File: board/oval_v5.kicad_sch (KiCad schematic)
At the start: 122 parts, among them J1 HDR-5x1, J10 HDR-4x1, J11 HDR-4x1, J12 HDR-4x1, J13 HDR-4x1, J14 HDR-4x1, J15 HDR-4x1, J16 HDR-4x1, J17 HDR-4x1, J18 Conn_Coaxial, J19 Conn_01x02, J2 HDR-4x1, J20 Conn_01x02, J21 Conn_02x02_Counter_Clockwise, J22 HDR-2x1, J23 HDR-2x1, J25 Conn_01x06, J3 HDR-4x1, J4 Conn_01x06, J5 Micro_SD_Card, J6 Conn_01x02, J7 HDR-4x1, J8 Conn_01x08, J9 HDR-4x1, P1 USB_C_Plug_USB2.0, Q1 Q_PMOS_GSD, Q2 MMBT3904, Q3 MMBT3904, SW1 SW_DIP_x02, SW2 SW_DIP_x02, U1 RV-8803, U10 SiP32431DR3, U11 SiP32431DR3, U12 SiP32431DR3, U13 SiP32431DR3, U14 SiP32431DR3, U15 PCF8574TS, U16 PCA9548APW, U17 SiP32431DR3, U2 ESP32-S3-WROOM-1, U3 TMP117xxDRV, U4 RFM95W-915S2, U7 MAX3485, U8 AP7361C-33E, U9 AP7361C-33E

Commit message: minor changes
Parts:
- D5: footprint Diode_SMD:D_SOD-323 -> Diode_SMD:D_SOD-323_HandSoldering
- J20: footprint Connector_PinHeader_2.54mm:PinHeader_1x02_P2.54mm_Vertical -> Connector_JST:JST_XH_B2B-XH-A_1x02_P2.50mm_Vertical
- J25, J4: footprint Connector_PinHeader_2.54mm:PinHeader_1x06_P2.54mm_Vertical -> Connector_JST:JST_XH_B6B-XH-A_1x06_P2.50mm_Vertical
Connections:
- net CLK is gone; now on net SPI_SCLK: R4.1, U4.4 (SCK)
- net MISO is gone; now on net SPI_MISO: R5.1, U4.2 (MISO)
- net MOSI is gone; now on net SPI_MOSI: R3.1, U4.3 (MOSI)
- net SIM_PWRKEY is gone; now on net GSM_PWRKEY: J25.3 (Pin_3)
- net SIM_RST is gone; now on net GSM_RST: J25.4 (Pin_4)
- net SIM_RX is gone; now on net GSM_Rx: J25.2 (Pin_2)
- net SIM_TX is gone; now on net GSM_Tx: J25.1 (Pin_1)
- net GSM_Rx: now also U2.10 (GPIO17/U1TXD/ADC2_CH6)
- net GSM_Tx: now also U2.11 (GPIO18/U1RXD/ADC2_CH7/CLK_OUT3)
- net RS485_EN: now also U2.25 (GPIO48/SPICLK_N/SUBSPICLK_N_DIFF)
- net rfm_RST: now also U2.5 (GPIO5/TOUCH5/ADC1_CH4); no longer U2.10 (GPIO17/U1TXD/ADC2_CH6)
- net rfm_dio1: now also U2.24 (GPIO47/SPICLK_P/SUBSPICLK_P_DIFF); no longer U2.11 (GPIO18/U1RXD/ADC2_CH7/CLK_OUT3)
- net rfm_dio2: now also U2.6 (GPIO6/TOUCH6/ADC1_CH5), U4.16 (DIO2); no longer U2.31 (GPIO38/FSPIWP/SUBSPIWP)
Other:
- moved on the sheet: J18, U4

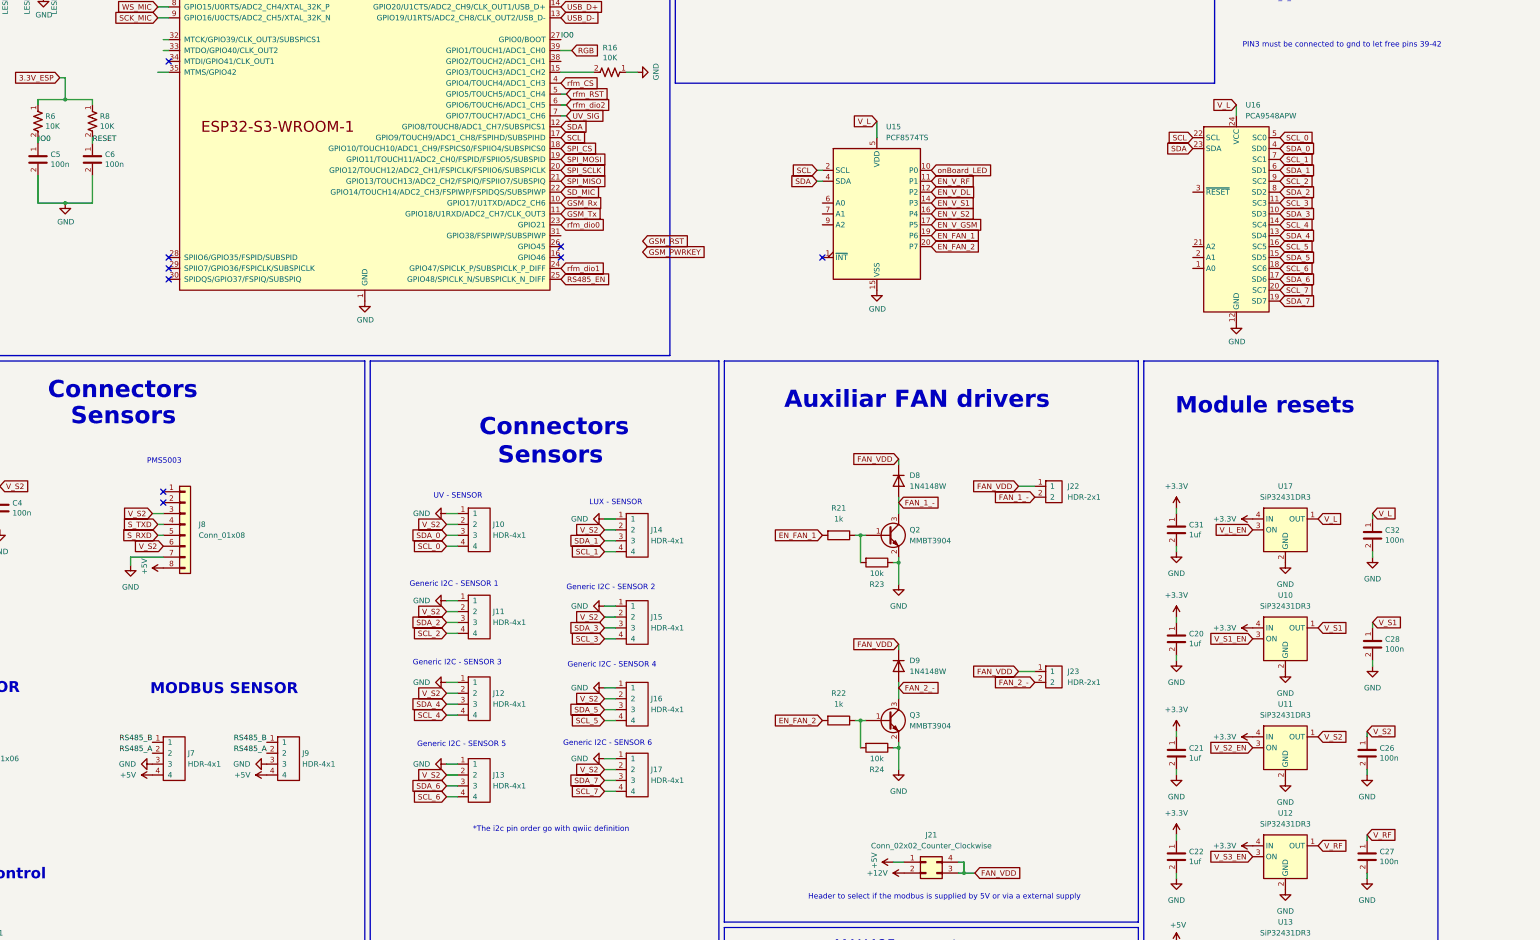
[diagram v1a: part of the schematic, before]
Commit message: working on layout -  defining connectors and cables
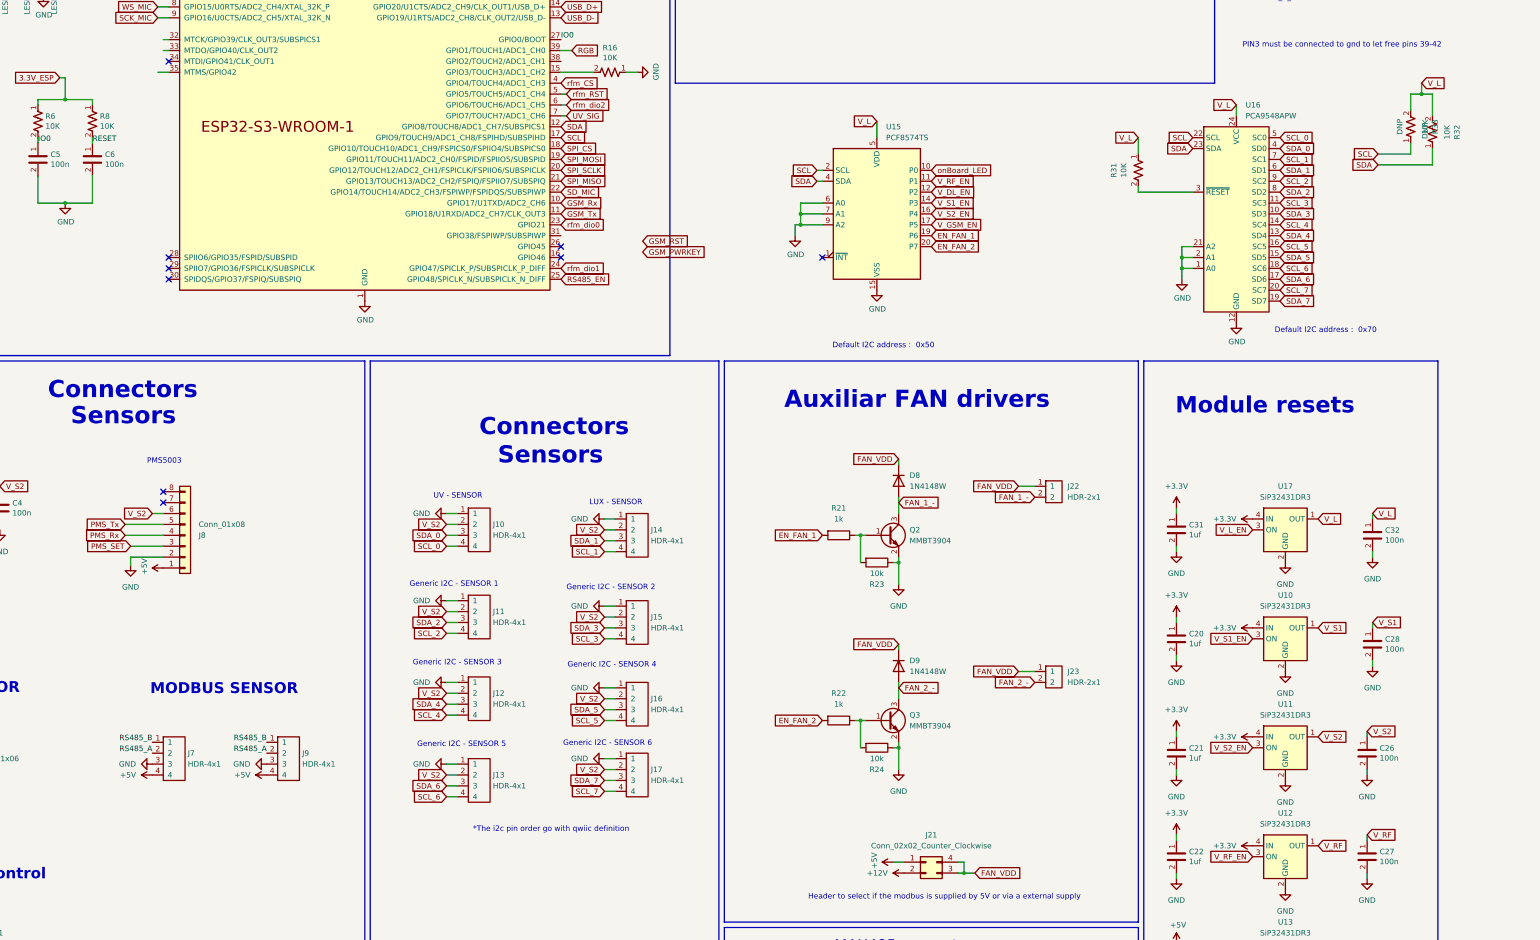
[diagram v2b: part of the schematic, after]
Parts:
- added R31, R32, R33: 10K, Resistor_SMD:R_0603_1608Metric, symbol IoWLabs:RES
- J4: footprint Connector_JST:JST_XH_B6B-XH-A_1x06_P2.50mm_Vertical -> Connector_JST:JST_GH_SM06B-GHS-TB_1x06-1MP_P1.25mm_Horizontal
- J8: footprint Connector_JST:JST_GH_SM08B-GHS-TB_1x08-1MP_P1.25mm_Horizontal -> Connector_Molex:Molex_PicoBlade_53261-0871_1x08-1MP_P1.25mm_Horizontal
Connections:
- net EN_V_DL is gone; now on net V_DL_EN: U15.12 (P2)
- net EN_V_GSM is gone; now on net V_GSM_EN: U15.17 (P5)
- net EN_V_S1 is gone; now on net V_S1_EN: U15.14 (P3)
- net EN_V_S2 is gone; now on net V_S2_EN: U15.16 (P4)
- net V_S3_EN is gone; now on net V_RF_EN: U12.3 (ON)
- net +5V: now also J8.1 (Pin_1); no longer J8.8 (Pin_8)
- net GND: now also J8.2 (Pin_2), U15.6 (A0), U15.7 (A1), U15.9 (A2), U16.1 (A0), U16.2 (A1), U16.21 (A2); no longer J8.7 (Pin_7)
- net SCL: now also R33.1
- net SDA: now also R32.1
- net V_L: now also R31.1, R32.2, R33.2
- net V_S2: no longer J8.3 (Pin_3)
- net at U16.3 (~{RESET}): now also R31.2
- net EN_V_RF renamed V_RF_EN
- net S_RXD renamed PMS_Tx
- net S_TXD renamed PMS_Rx
- new net PMS_SET: J8.3 (Pin_3)
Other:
- note added: "Default I2C address : 0x50"
- note added: "Default I2C address : 0x70"

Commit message: assignint pines
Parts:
- removed U15: PCF8574TS, Package_SO:SSOP-20_4.4x6.5mm_P0.65mm, symbol Interface_Expansion:PCF8574TS
- added C33: 100n, Capacitor_SMD:C_0603_1608Metric, symbol IoWLabs:C
- added C34: 10u, Capacitor_SMD:C_0805_2012Metric, symbol IoWLabs:C
- added R34, R35: 10k, Resistor_SMD:R_0603_1608Metric, symbol Device:R
- added R36, R37: 10K, Resistor_SMD:R_0603_1608Metric, symbol IoWLabs:RES
- added U18: PCA9555PW, Package_SO:TSSOP-24_4.4x7.8mm_P0.65mm, symbol Interface_Expansion:PCA9555PW
- R10, R11: value 2.2k -> 10k
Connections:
- net SPI_CS is gone; now on net SD_CS: U2.18 (GPIO10/TOUCH10/ADC1_CH9/FSPICS0/FSPIIO4/SUBSPICS0)
- net EN_FAN_1: now also U18.10 (IO0_6)
- net EN_FAN_2: now also U18.11 (IO0_7)
- net GND: now also C33.2, C34.2, U18.12 (VSS), U18.2 (A1), U18.21 (A0), U18.3 (A2)
- net GSM_PWRKEY: now also U2.6 (GPIO6/TOUCH6/ADC1_CH5)
- net GSM_RST: now also U2.5 (GPIO5/TOUCH5/ADC1_CH4)
- net PMS_Rx: now also U2.35 (MTMS/GPIO42)
- net PMS_SET: now also U18.13 (IO1_0)
- net PMS_Tx: now also U2.34 (MTDI/GPIO41/CLK_OUT1)
- net RS485_EN: now also U18.14 (IO1_1); no longer U2.25 (GPIO48/SPICLK_N/SUBSPICLK_N_DIFF)
- net SCL: now also R35.2, R36.1, U18.22 (SCL)
- net SDA: now also R34.2, R37.1, U18.23 (SDA)
- net V_DL_EN: now also U18.6 (IO0_2)
- net V_GSM_EN: now also U18.9 (IO0_5)
- net V_L: now also C33.1, C34.1, R36.2, R37.2, U18.24 (VDD)
- net V_RF_EN: now also U18.5 (IO0_1)
- net V_S1_EN: now also U18.7 (IO0_3)
- net V_S2: now also R34.1, R35.1
- net V_S2_EN: now also U18.8 (IO0_4)
- net onBoard_LED: now also U18.4 (IO0_0)
- net rfm_CS: now also U2.33 (MTDO/GPIO40/CLK_OUT2); no longer U2.4 (GPIO4/TOUCH4/ADC1_CH3)
- net rfm_RST: now also U2.32 (MTCK/GPIO39/CLK_OUT3/SUBSPICS1); no longer U2.5 (GPIO5/TOUCH5/ADC1_CH4)
- net rfm_dio0: now also U2.31 (GPIO38/FSPIWP/SUBSPIWP); no longer U2.23 (GPIO21)
- net rfm_dio2: now also U2.25 (GPIO48/SPICLK_N/SUBSPICLK_N_DIFF); no longer U2.6 (GPIO6/TOUCH6/ADC1_CH5)
- no-connect marks 23 -> 21
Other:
- note added: "Default I2C address : 0x20"
- note removed: "Default I2C address : 0x50"
- moved on the sheet: C5, C6, J4, J7, J9, R6, R8

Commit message: updateing 27/02
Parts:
- J1: footprint Connector_JST:JST_XH_B5B-XH-A_1x05_P2.50mm_Vertical -> Connector_JST:JST_PH_B5B-PH-K_1x05_P2.00mm_Vertical
- J10, J11, J12, J13, J14, J15, J16, J17: footprint Connector_JST:JST_SH_BM04B-SRSS-TB_1x04-1MP_P1.00mm_Vertical -> Connector_JST:JST_PH_B4B-PH-K_1x04_P2.00mm_Vertical
- J2, J3: footprint Connector_JST:JST_XH_B4B-XH-A_1x04_P2.50mm_Vertical -> Connector_JST:JST_SH_BM04B-SRSS-TB_1x04-1MP_P1.00mm_Vertical
- J20: footprint Connector_JST:JST_XH_B2B-XH-A_1x02_P2.50mm_Vertical -> Connector_JST:JST_PH_B2B-PH-K_1x02_P2.00mm_Vertical
- J22, J23: footprint Connector_JST:JST_XH_B2B-XH-A_1x02_P2.50mm_Vertical -> Connector_JST:JST_PH_S2B-PH-SM4-TB_1x02-1MP_P2.00mm_Horizontal
- J7, J9: footprint Connector_JST:JST_XH_B4B-XH-A_1x04_P2.50mm_Vertical -> Connector_JST:JST_PH_B4B-PH-K_1x04_P2.00mm_Vertical
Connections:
- net V_L_EN: now also U2.23 (GPIO21)
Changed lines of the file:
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@@
 		)
 	)
+	(global_label "V_L_EN"
+		(shape input)
+		(at 187.96 134.62 0)
+		(fields_autoplaced yes)
+		(effects
+			(font
+				(size 1.27 1.27)
+			)
+			(justify left)
+		)
+		(property "Intersheetrefs" "${INTERSHEET_REFS}"
+			(at 197.4766 134.62 0)
+			(effects
+				(font
+					(size 1.27 1.27)
+				)
+				(justify left)
+				(hide yes)
+			)
+		)
+	)
 	(global_label "V_RF"
 		(shape input)
@@
 			)
 		)
-		(property "Footprint" "Connector_JST:JST_SH_BM04B-SRSS-TB_1x04-1MP_P1.00mm_Vertical"
+		(property "Footprint" "Connector_JST:JST_PH_B4B-PH-K_1x04_P2.00mm_Vertical"
 			(at 207.01 200.66 0)
 			(effects
@@
 			)
 		)
-		(property "Footprint" "Connector_JST:JST_SH_BM04B-SRSS-TB_1x04-1MP_P1.00mm_Vertical"
+		(property "Footprint" "Connector_JST:JST_PH_B4B-PH-K_1x04_P2.00mm_Vertical"
 			(at 170.18 238.76 0)
 			(effects
@@
 			)
 		)
-		(property "Footprint" "Connector_JST:JST_SH_BM04B-SRSS-TB_1x04-1MP_P1.00mm_Vertical"
+		(property "Footprint" "Connector_JST:JST_PH_B4B-PH-K_1x04_P2.00mm_Vertical"
 			(at 207.01 256.54 0)
 			(effects
@@
 			)
 		)
-		(property "Footprint" "Connector_JST:JST_XH_B4B-XH-A_1x04_P2.50mm_Vertical"
+		(property "Footprint" "Connector_JST:JST_PH_B4B-PH-K_1x04_P2.00mm_Vertical"
 			(at 101.6 251.46 0)
 			(effects
@@
 			)
 		)
-		(property "Footprint" "Connector_JST:JST_XH_B4B-XH-A_1x04_P2.50mm_Vertical"
+		(property "Footprint" "Connector_JST:JST_PH_B4B-PH-K_1x04_P2.00mm_Vertical"
 			(at 128.27 251.46 0)
 			(effects
@@
 			)
 		)
-		(property "Footprint" "Connector_JST:JST_SH_BM04B-SRSS-TB_1x04-1MP_P1.00mm_Vertical"
+		(property "Footprint" "Connector_JST:JST_PH_B4B-PH-K_1x04_P2.00mm_Vertical"
 			(at 170.18 257.81 0)
 			(effects
@@
 			)
 		)
-		(property "Footprint" "Connector_JST:JST_SH_BM04B-SRSS-TB_1x04-1MP_P1.00mm_Vertical"
+		(property "Footprint" "Connector_JST:JST_PH_B4B-PH-K_1x04_P2.00mm_Vertical"
 			(at 170.18 199.39 0)
 			(effects
@@
 			)
 		)
-		(property "Footprint" "Connector_JST:JST_XH_B2B-XH-A_1x02_P2.50mm_Vertical"
+		(property "Footprint" "Connector_JST:JST_PH_S2B-PH-SM4-TB_1x02-1MP_P2.00mm_Horizontal"
 			(at 302.26 236.22 0)
 			(effects
@@
 			)
 		)
-		(property "Footprint" "Connector_JST:JST_SH_BM04B-SRSS-TB_1x04-1MP_P1.00mm_Vertical"
+		(property "Footprint" "Connector_JST:JST_PH_B4B-PH-K_1x04_P2.00mm_Vertical"
 			(at 207.01 220.98 0)
 			(effects
@@
 			)
 		)
-		(property "Footprint" "Connector_JST:JST_SH_BM04B-SRSS-TB_1x04-1MP_P1.00mm_Vertical"
+		(property "Footprint" "Connector_JST:JST_PH_B4B-PH-K_1x04_P2.00mm_Vertical"
 			(at 170.18 219.71 0)
 			(effects
@@
 			)
 		)
-		(property "Footprint" "Connector_JST:JST_XH_B4B-XH-A_1x04_P2.50mm_Vertical"
+		(property "Footprint" "Connector_JST:JST_SH_BM04B-SRSS-TB_1x04-1MP_P1.00mm_Vertical"
 			(at 46.99 219.71 0)
 			(effects
@@
 			)
 		)
-		(property "Footprint" "Connector_JST:JST_XH_B2B-XH-A_1x02_P2.50mm_Vertical"
+		(property "Footprint" "Connector_JST:JST_PH_S2B-PH-SM4-TB_1x02-1MP_P2.00mm_Horizontal"
 			(at 302.26 193.04 0)
 			(effects
@@
 			)
 		)
-		(property "Footprint" "Connector_JST:JST_SH_BM04B-SRSS-TB_1x04-1MP_P1.00mm_Vertical"
+		(property "Footprint" "Connector_JST:JST_PH_B4B-PH-K_1x04_P2.00mm_Vertical"
 			(at 207.01 240.03 0)
 			(effects
@@
 			)
 		)
-		(property "Footprint" "Connector_JST:JST_XH_B2B-XH-A_1x02_P2.50mm_Vertical"
+		(property "Footprint" "Connector_JST:JST_PH_B2B-PH-K_1x02_P2.00mm_Vertical"
 			(at 269.24 35.56 0)
 			(effects
@@
 			)
 		)
-		(property "Footprint" "Connector_JST:JST_XH_B5B-XH-A_1x05_P2.50mm_Vertical"
+		(property "Footprint" "Connector_JST:JST_PH_B5B-PH-K_1x05_P2.00mm_Vertical"
 			(at 44.45 209.55 0)
 			(effects
@@
 			)
 		)
-		(property "Footprint" "Connector_JST:JST_XH_B4B-XH-A_1x04_P2.50mm_Vertical"
+		(property "Footprint" "Connector_JST:JST_SH_BM04B-SRSS-TB_1x04-1MP_P1.00mm_Vertical"
 			(at 48.26 292.1 0)
 			(effects

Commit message: adding layout review
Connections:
- net GSM_PWRKEY: now also U2.35 (MTMS/GPIO42); no longer U2.6 (GPIO6/TOUCH6/ADC1_CH5)
- net GSM_RST: now also U2.32 (MTCK/GPIO39/CLK_OUT3/SUBSPICS1); no longer U2.5 (GPIO5/TOUCH5/ADC1_CH4)
- net PMS_Rx: now also U2.33 (MTDO/GPIO40/CLK_OUT2); no longer U2.35 (MTMS/GPIO42)
- net SCK_MIC: no longer U2.9 (GPIO16/U0CTS/ADC2_CH5/XTAL_32K_N)
- net SD_MIC: no longer U2.22 (GPIO14/TOUCH14/ADC2_CH3/FSPIWP/FSPIDQS/SUBSPIWP)
- net WS_MIC: no longer U2.8 (GPIO15/U0RTS/ADC2_CH4/XTAL_32K_P)
- net rfm_CS: now also U2.4 (GPIO4/TOUCH4/ADC1_CH3); no longer U2.33 (MTDO/GPIO40/CLK_OUT2)
- net rfm_RST: now also U2.5 (GPIO5/TOUCH5/ADC1_CH4); no longer U2.32 (MTCK/GPIO39/CLK_OUT3/SUBSPICS1)
- net rfm_dio0: now also U2.6 (GPIO6/TOUCH6/ADC1_CH5)
- new net MIC_SCK: U2.9 (GPIO16/U0CTS/ADC2_CH5/XTAL_32K_N)
- new net MIC_SD: U2.22 (GPIO14/TOUCH14/ADC2_CH3/FSPIWP/FSPIDQS/SUBSPIWP)
- new net MIC_WS: U2.8 (GPIO15/U0RTS/ADC2_CH4/XTAL_32K_P)
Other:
- note added: "ESP32 USED SIGNALS - PINs ---------------------- GPIO44 - RS485Tx GPIO43 - RS485Rx GPIO08 - SDA GPIO09 - SCL GPIO10 - SD_CS GPIO11 - MOSI GPIO12 - SCLK GPIO13 - MISO GPIO04 - rfm_CS GPIO05 - rfm_RST GPIO06 - rfm_dio0 GPIO47 - rfm_dio1 GPIO48 - rfm_dio2 GPIO01 - RGB GPIO15 - MIC_WS GPIO16 - MIC_SCK GPIO14 - MIC_SD GPIO07 - UV_SIG GPIO39 - GSM_RST GPIO42 - GSM_PWRKEY GPIO18 - GSM_Tx GPIO17 - GSM_Rx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"
- note added: "Expansor GPIO ------------------- GPIO00 - onBoardLED GPIO01 - V_GSM_EN GPIO02 - V_S1_EN GPIO03 - V_S2_EN GPIO04 - V_RF_EN GPIO05 - V_DL_EN GPIO06 - FAN_1_EN GPIO07 - FAN_1_EN GPIO08 - PMS_SET GPIO09 - RS485_EN"
- note removed: "ESP32 USED SIGNALS - PINs ---------------------- GPIO44 - RS485Tx GPIO43 - RS485Rx GPIO42 - RS485EN GPIO04 - rfm_CS GPIO08 - SDA GPIO09 - SCL GPIO10 - SD_CS GPIO11 - MOSI GPIO12 - SCLK GPIO13 - MISO GPIO01 - RGB GPIO02 - onBoardLED GPIO05 - EN_V_RF GPIO06 - EN_V_DL GPIO47 - EN_FAN_1 GPIO48 - EN_FAN_2 GPIO15 - WS_MIC GPIO16 - SCK_MIC GPIO14 - SD_MIC GPIO07 - UV_SIG GPIO17 - rfm_RST GPIO18 - rfm_di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"
- note removed: "Expansor GPIO ------------------- GPIO00 - onBoardLED GPIO01 - EN_V_RF GPIO02 - EN_V_DL GPIO06 - EN_FAN_1 GPIO07 - EN_FAN_2 GPIO03 - EN_V_S1 GPIO04 - EN_V_S2 GPIO05 - EN_V_GSM"
- moved on the sheet: C33, C34, R31, R32, R33, R36, R37, U16, U18
